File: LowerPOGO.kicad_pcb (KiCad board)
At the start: 2 copper layers, 116 x 58 mm, 34 parts, among them J1 Conn_01x01_MountingPin, J10 Conn_01x01_MountingPin, J11 Conn_01x01_MountingPin, J12 Conn_01x01_MountingPin, J13 Conn_01x01_MountingPin, J14 Conn_01x01_MountingPin, J15 Conn_01x01_MountingPin, J16 Conn_01x01_MountingPin, J17 Conn_01x01_MountingPin, J18 Conn_01x01_MountingPin, J19 Conn_01x01_MountingPin, J2 Conn_01x01_MountingPin, J20 Conn_01x01_MountingPin, J21 Conn_01x01_MountingPin, J22 Conn_01x01_MountingPin, J23 Conn_01x01_MountingPin, J24 Conn_01x01_MountingPin, J25 Conn_01x04_Pin, J26 Conn_01x04_Pin, J27 Conn_01x04_Pin, J28 Conn_01x04_Pin, J29 Conn_01x04_Pin, J3 Conn_01x01_MountingPin, J30 Conn_01x04_Pin, J4 Conn_01x01_MountingPin, J5 Conn_01x01_MountingPin, J6 Conn_01x01_MountingPin, J7 Conn_01x01_MountingPin, J8 Conn_01x01_MountingPin, J9 Conn_01x01_MountingPin

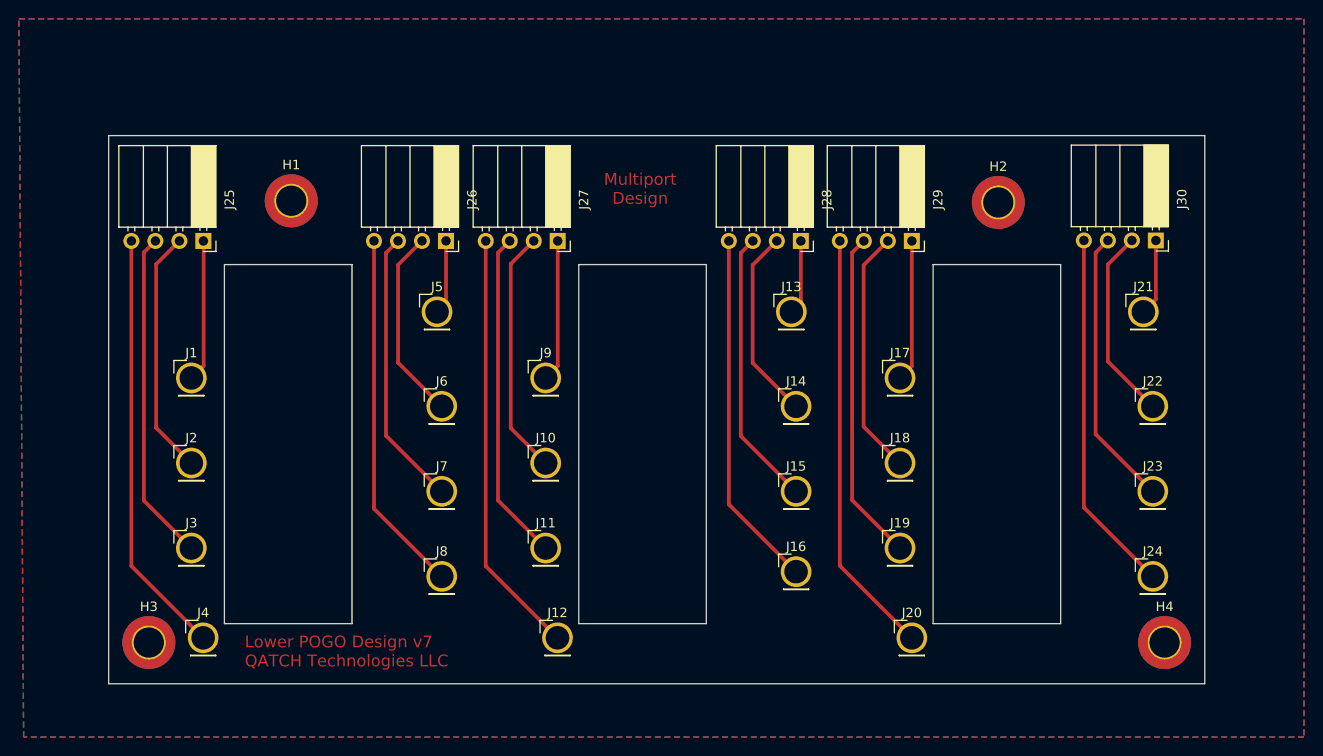
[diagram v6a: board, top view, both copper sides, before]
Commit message: LowerPOGO v8 Changes: - Flip lower POGO design for modified sensor layout
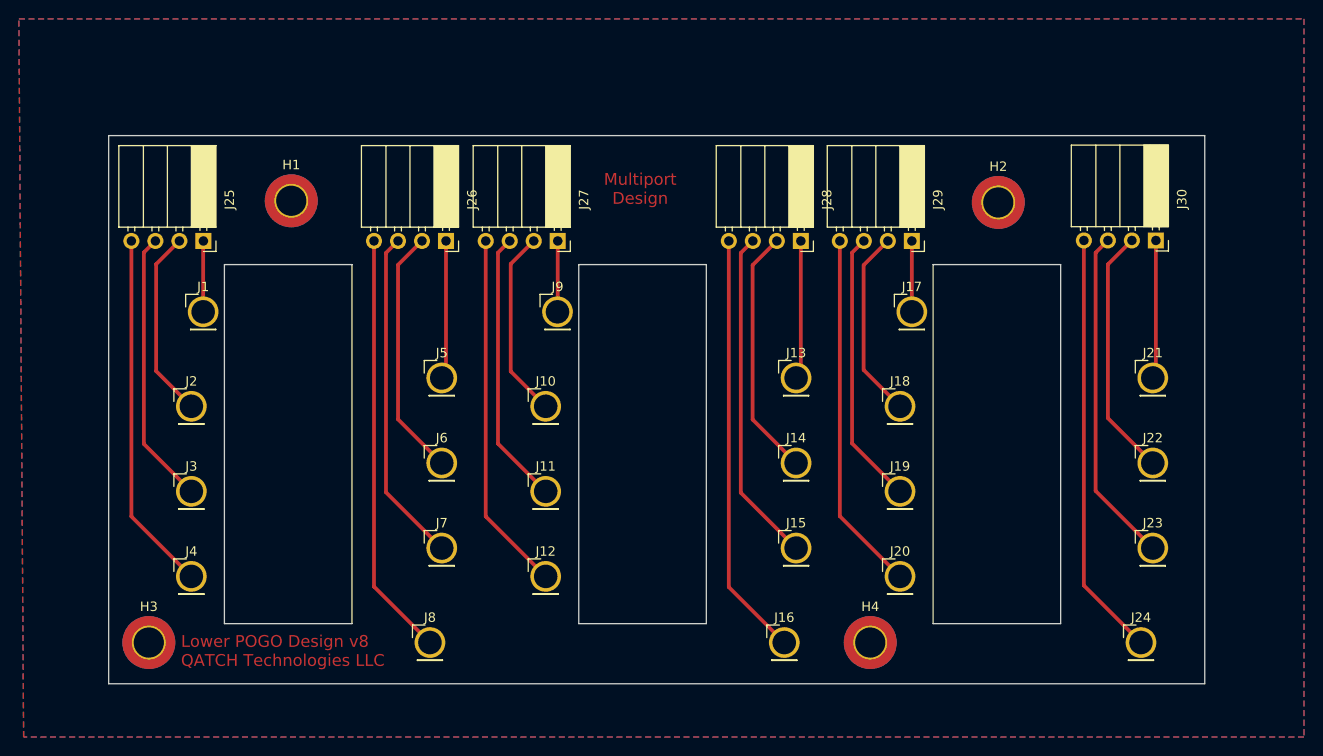
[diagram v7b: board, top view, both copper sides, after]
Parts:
- moved H4 31.2 mm to (169.6, 154.5)
- moved J16 7.60 mm to (160.5, 154.5)
- moved J1 7.11 mm to (99.0, 119.5)
- moved J17 7.11 mm to (174.0, 119.5)
- moved J24 7.11 mm to (198.2, 154.5)
- moved J8 7.11 mm to (123.0, 154.5)
- moved J9 7.11 mm to (136.5, 119.5)
- moved J21 7.07 mm to (199.5, 126.5)
- moved J13 7.02 mm to (161.8, 126.5)
- moved J5 7.02 mm to (124.2, 126.5)
- moved J12 6.62 mm to (135.2, 147.5)
- moved J20 6.62 mm to (172.8, 147.5)
- moved J4 6.62 mm to (97.8, 147.5)
- moved J10 6.00 mm to (135.2, 129.5)
- moved J11 6.00 mm to (135.2, 138.5)
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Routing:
- net Net-(J27-Pin_1): track 15.0 -> 7.51 mm
- net Net-(J17-Pin_1): track 15.0 -> 7.50 mm
- net Net-(J1-Pin_1): track 15.0 -> 7.55 mm
- net Net-(J25-Pin_4): track 45.1 -> 38.1 mm
- net Net-(J20-Pin_1): track 45.2 -> 38.1 mm
- net Net-(J12-Pin_1): track 45.1 -> 38.1 mm
- net Net-(J16-Pin_1): track 37.9 -> 44.9 mm
- net Net-(J13-Pin_1): track 7.91 -> 14.7 mm
- net Net-(J26-Pin_1): track 7.89 -> 14.7 mm
- net Net-(J21-Pin_1): track 8.10 -> 14.7 mm
- net Net-(J26-Pin_4): track 38.5 -> 45.0 mm
- net Net-(J24-Pin_1): track 38.6 -> 45.1 mm
- net Net-(J18-Pin_1): track 26.2 -> 20.2 mm
- net Net-(J10-Pin_1): track 26.0 -> 20.0 mm
- net Net-(J26-Pin_2): track 20.5 -> 26.5 mm
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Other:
- board text added: "Lower POGO Design v8 QATCH Technologies LLC"
- board text removed: "Lower POGO Design v7 QATCH Technologies LLC"
